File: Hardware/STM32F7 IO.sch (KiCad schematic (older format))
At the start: 26 parts, among them U16 STM32F765ZGT6

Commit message: Fixed serge suggestions
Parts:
- added TP?: TEST, Measurement_Points:Measurement_Point_Round-SMD-Pad_Big, symbol TEST
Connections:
- wire segments 183 -> 184
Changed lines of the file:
@@
 $Descr A4 11693 8268
 encoding utf-8
-Sheet 17 20
+Sheet 17 21
 Title "Autopilot Controller I/O"
 Date "2017-05-14"
@@
 $EndComp
 $Comp
-L GND #PWR48
+L GND #PWR046
 U 1 1 591E59BE
 P 10600 6000
-F 0 "#PWR48" H 10600 5750 50  0001 C CNN
+F 0 "#PWR046" H 10600 5750 50  0001 C CNN
 F 1 "GND" H 10600 5850 50  0000 C CNN
 F 2 "" H 10600 6000 50  0001 C CNN
@@
 $EndComp
 $Comp
-L GND #PWR46
+L GND #PWR047
 U 1 1 591EB43A
 P 6650 6500
-F 0 "#PWR46" H 6650 6250 50  0001 C CNN
+F 0 "#PWR047" H 6650 6250 50  0001 C CNN
 F 1 "GND" H 6650 6350 50  0000 C CNN
 F 2 "" H 6650 6500 50  0001 C CNN
@@
 Connection ~ 8550 2550
 $Comp
-L GND #PWR47
+L GND #PWR048
 U 1 1 59530E80
 P 8550 2600
-F 0 "#PWR47" H 8550 2350 50  0001 C CNN
+F 0 "#PWR048" H 8550 2350 50  0001 C CNN
 F 1 "GND" H 8550 2450 50  0000 C CNN
 F 2 "" H 8550 2600 50  0001 C CNN
@@
 L STM32F765ZGT6 U16
 U 8 1 595F8E91
-P 9500 5050
-F 0 "U16" H 9500 5950 60  0000 C CNN
-F 1 "STM32F765ZGT6" H 9500 5800 60  0000 C CNN
-F 2 "Housings_QFP:LQFP-144_20x20mm_Pitch0.5mm" H 10550 5150 60  0001 C CNN
-F 3 "" H 10550 5150 60  0001 C CNN
-F 4 "CHIP-001" H 9600 6050 60  0000 C CNN "part_num"
-	8    9500 5050
-	1    0    0    -1
+P 9600 5050
+F 0 "U16" H 9600 5950 60  0000 C CNN
+F 1 "STM32F765ZGT6" H 9600 5800 60  0000 C CNN
+F 2 "Housings_QFP:LQFP-144_20x20mm_Pitch0.5mm" H 10650 5150 60  0001 C CNN
+F 3 "" H 10650 5150 60  0001 C CNN
+F 4 "CHIP-001" H 9700 6050 60  0000 C CNN "part_num"
+	8    9600 5050
+	-1   0    0    -1
 $EndComp
 $Comp
@@
 	1    0    0    -1
 $EndComp
+$Comp
+L TEST TP?
+U 1 1 596A0986
+P 10450 2900
+F 0 "TP?" H 10450 3200 50  0000 C BNN
+F 1 "TEST" H 10450 3150 50  0000 C CNN
+F 2 "Measurement_Points:Measurement_Point_Round-SMD-Pad_Big" H 10450 2900 50  0001 C CNN
+F 3 "" H 10450 2900 50  0001 C CNN
+	1    10450 2900
+	1    0    0    -1
+$EndComp
+Wire Wire Line
+	10450 2900 10050 2900
 $EndSCHEMATC

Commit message: commit before my computer restarts
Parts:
- gave numbers to parts that had none: 1
- renumbered D17 to D15, D18 to D16, D19 to D17, R78 to R36, R79 to R37, R80 to R38, R81 to R39
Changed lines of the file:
@@
 VDD
 $Comp
-L LED D18
+L LED D16
 U 1 1 5952F90F
 P 8550 1950
-F 0 "D18" H 8550 2050 50  0000 C CNN
+F 0 "D16" H 8550 2050 50  0000 C CNN
 F 1 "LED" H 8550 1850 50  0000 C CNN
 F 2 "LEDs:LED_0603" H 8550 1950 50  0001 C CNN
@@
 $EndComp
 $Comp
-L LED D19
+L LED D17
 U 1 1 5952FA63
 P 8800 1950
-F 0 "D19" H 8800 2050 50  0000 C CNN
+F 0 "D17" H 8800 2050 50  0000 C CNN
 F 1 "LED" H 8800 1850 50  0000 C CNN
 F 2 "LEDs:LED_0603" H 8800 1950 50  0001 C CNN
@@
 $EndComp
 $Comp
-L LED D17
+L LED D15
 U 1 1 5952FAD9
 P 8300 1950
-F 0 "D17" H 8300 2050 50  0000 C CNN
+F 0 "D15" H 8300 2050 50  0000 C CNN
 F 1 "LED" H 8300 1850 50  0000 C CNN
 F 2 "LEDs:LED_0603" H 8300 1950 50  0001 C CNN
@@
 	7500 1450 7050 1450
 $Comp
-L R R78
+L R R36
 U 1 1 59530176
 P 8300 2300
-F 0 "R78" V 8380 2300 50  0000 C CNN
+F 0 "R36" V 8380 2300 50  0000 C CNN
 F 1 "100" V 8300 2300 50  0000 C CNN
 F 2 "Resistors_SMD:R_0603_HandSoldering" V 8230 2300 50  0001 C CNN
@@
 $EndComp
 $Comp
-L R R79
+L R R37
 U 1 1 5959BB88
 P 8550 2300
-F 0 "R79" V 8630 2300 50  0000 C CNN
+F 0 "R37" V 8630 2300 50  0000 C CNN
 F 1 "100" V 8550 2300 50  0000 C CNN
 F 2 "Resistors_SMD:R_0603_HandSoldering" V 8480 2300 50  0001 C CNN
@@
 $EndComp
 $Comp
-L R R80
+L R R38
 U 1 1 5959BBE4
 P 8800 2300
-F 0 "R80" V 8880 2300 50  0000 C CNN
+F 0 "R38" V 8880 2300 50  0000 C CNN
 F 1 "100" V 8800 2300 50  0000 C CNN
 F 2 "Resistors_SMD:R_0603_HandSoldering" V 8730 2300 50  0001 C CNN
@@
 $EndComp
 $Comp
-L R R81
+L R R39
 U 1 1 595F2290
 P 10550 3000
-F 0 "R81" V 10630 3000 50  0000 C CNN
+F 0 "R39" V 10630 3000 50  0000 C CNN
 F 1 "0" V 10550 3000 50  0000 C CNN
 F 2 "Resistors_SMD:R_0603_HandSoldering" V 10480 3000 50  0001 C CNN
@@
 $EndComp
 $Comp
-L TEST TP?
+L TEST TP39
 U 1 1 596A0986
 P 10450 2900
-F 0 "TP?" H 10450 3200 50  0000 C BNN
+F 0 "TP39" H 10450 3200 50  0000 C BNN
 F 1 "TEST" H 10450 3150 50  0000 C CNN
 F 2 "Measurement_Points:Measurement_Point_Round-SMD-Pad_Big" H 10450 2900 50  0001 C CNN

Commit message: routed PWM and SEL bus
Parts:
- TP39: footprint Measurement_Points:Measurement_Point_Round-SMD-Pad_Big -> Measurement_Points:Measurement_Point_Round-SMD-Pad_Small
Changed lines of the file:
@@
 F 0 "TP39" H 10450 3200 50  0000 C BNN
 F 1 "TEST" H 10450 3150 50  0000 C CNN
-F 2 "Measurement_Points:Measurement_Point_Round-SMD-Pad_Big" H 10450 2900 50  0001 C CNN
+F 2 "Measurement_Points:Measurement_Point_Round-SMD-Pad_Small" H 10450 2900 50  0001 C CNN
 F 3 "" H 10450 2900 50  0001 C CNN
 	1    10450 2900

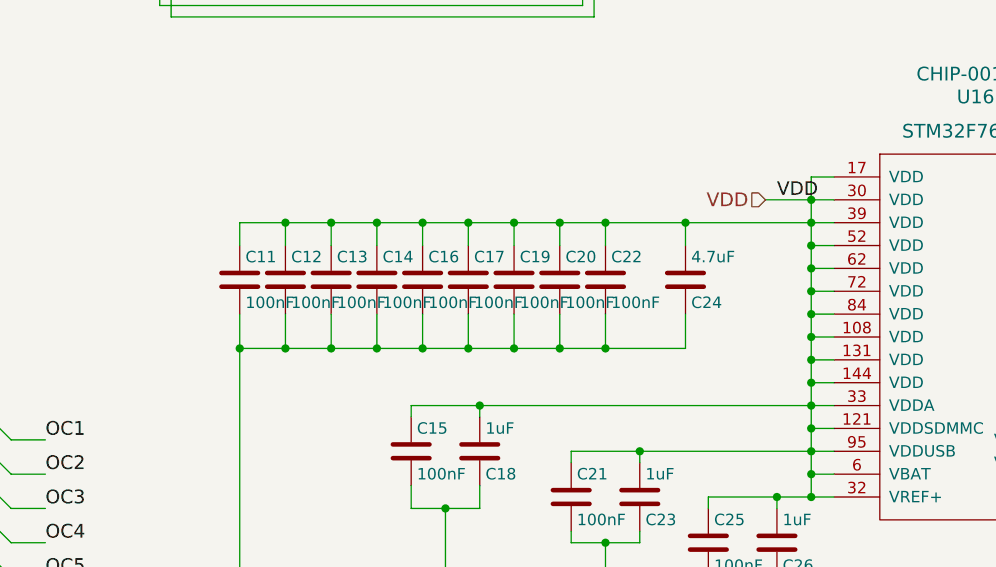
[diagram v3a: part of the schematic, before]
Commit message: placed headers in roughly correct spot
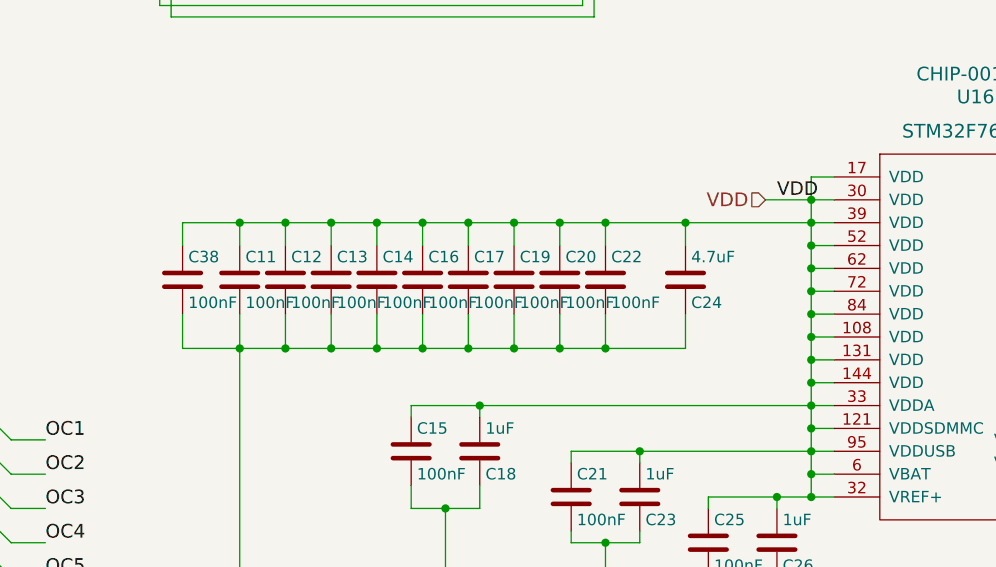
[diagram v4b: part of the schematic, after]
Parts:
- added C38: 100nF, Resistors_SMD:R_0603_HandSoldering, symbol C
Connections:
- net GND: now also C38.2
- net VDD: now also C38.1
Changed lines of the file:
@@
 	7950 5250 7950 5100
 Wire Wire Line
-	6350 5250 8300 5250
+	6100 5250 8300 5250
 Wire Wire Line
 	6350 5100 6350 6350
@@
 Connection ~ 8850 5300
 Wire Wire Line
-	6350 4700 8950 4700
+	6100 4700 8950 4700
 Connection ~ 8850 5400
 Wire Wire Line
@@
 Wire Wire Line
 	10450 2900 10050 2900
+$Comp
+L C C38
+U 1 1 592EA63D
+P 6100 4950
+F 0 "C38" H 6125 5050 50  0000 L CNN
+F 1 "100nF" H 6125 4850 50  0000 L CNN
+F 2 "Resistors_SMD:R_0603_HandSoldering" H 6138 4800 50  0001 C CNN
+F 3 "" H 6100 4950 50  0001 C CNN
+F 4 "CAPP-005" H 6100 4950 60  0001 C CNN "part_num"
+	1    6100 4950
+	1    0    0    -1
+$EndComp
+Wire Wire Line
+	6100 4700 6100 4800
+Connection ~ 6350 4700
+Wire Wire Line
+	6100 5100 6100 5250
 $EndSCHEMATC

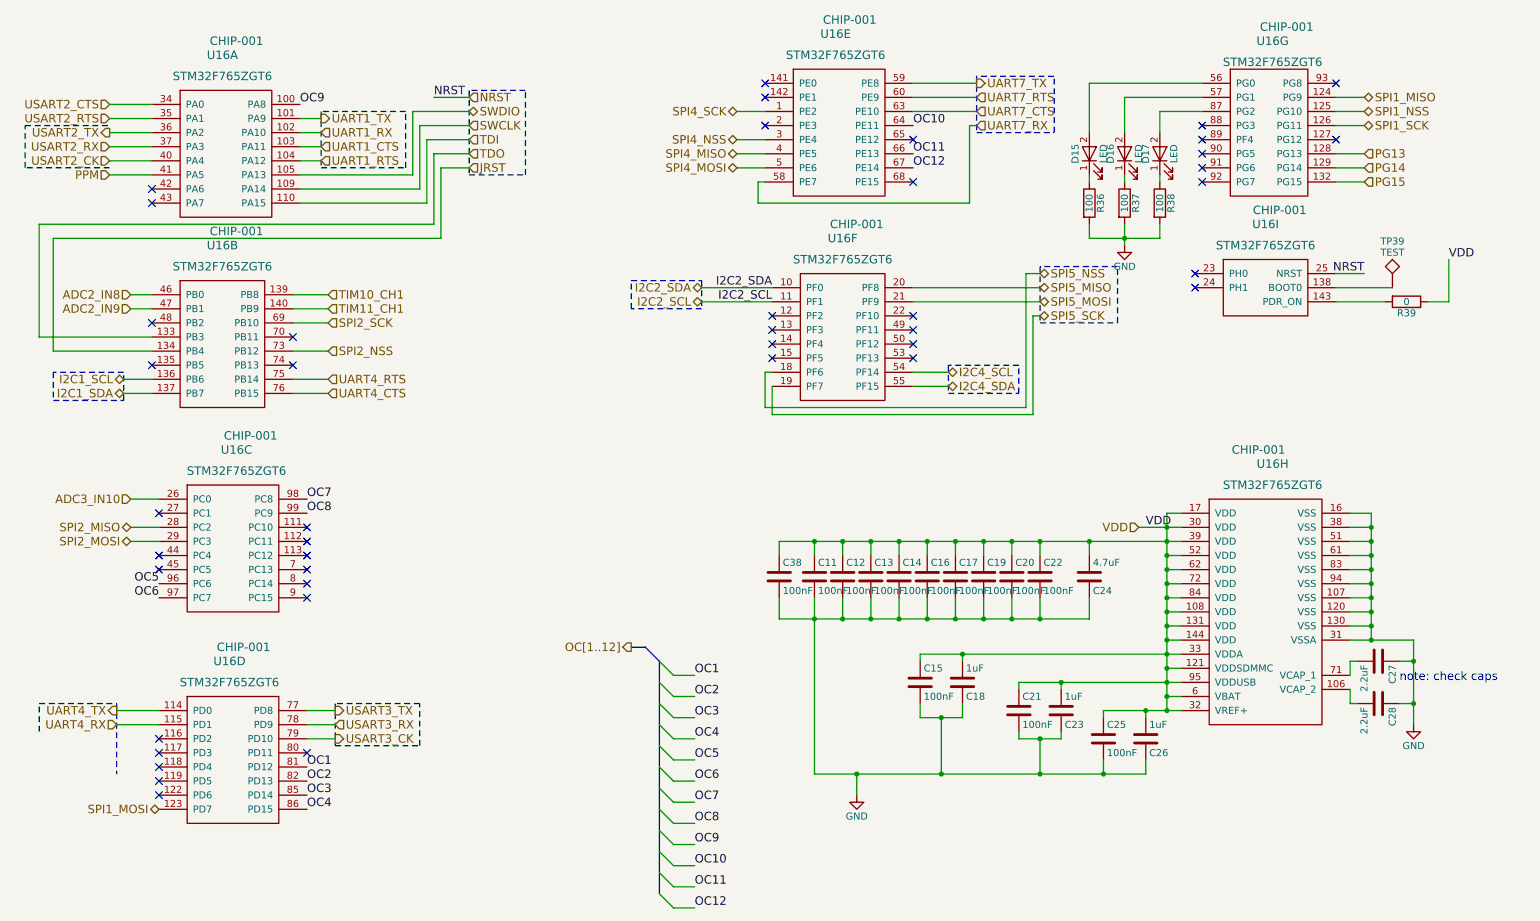
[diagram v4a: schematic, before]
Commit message: adc routing, made board smaller
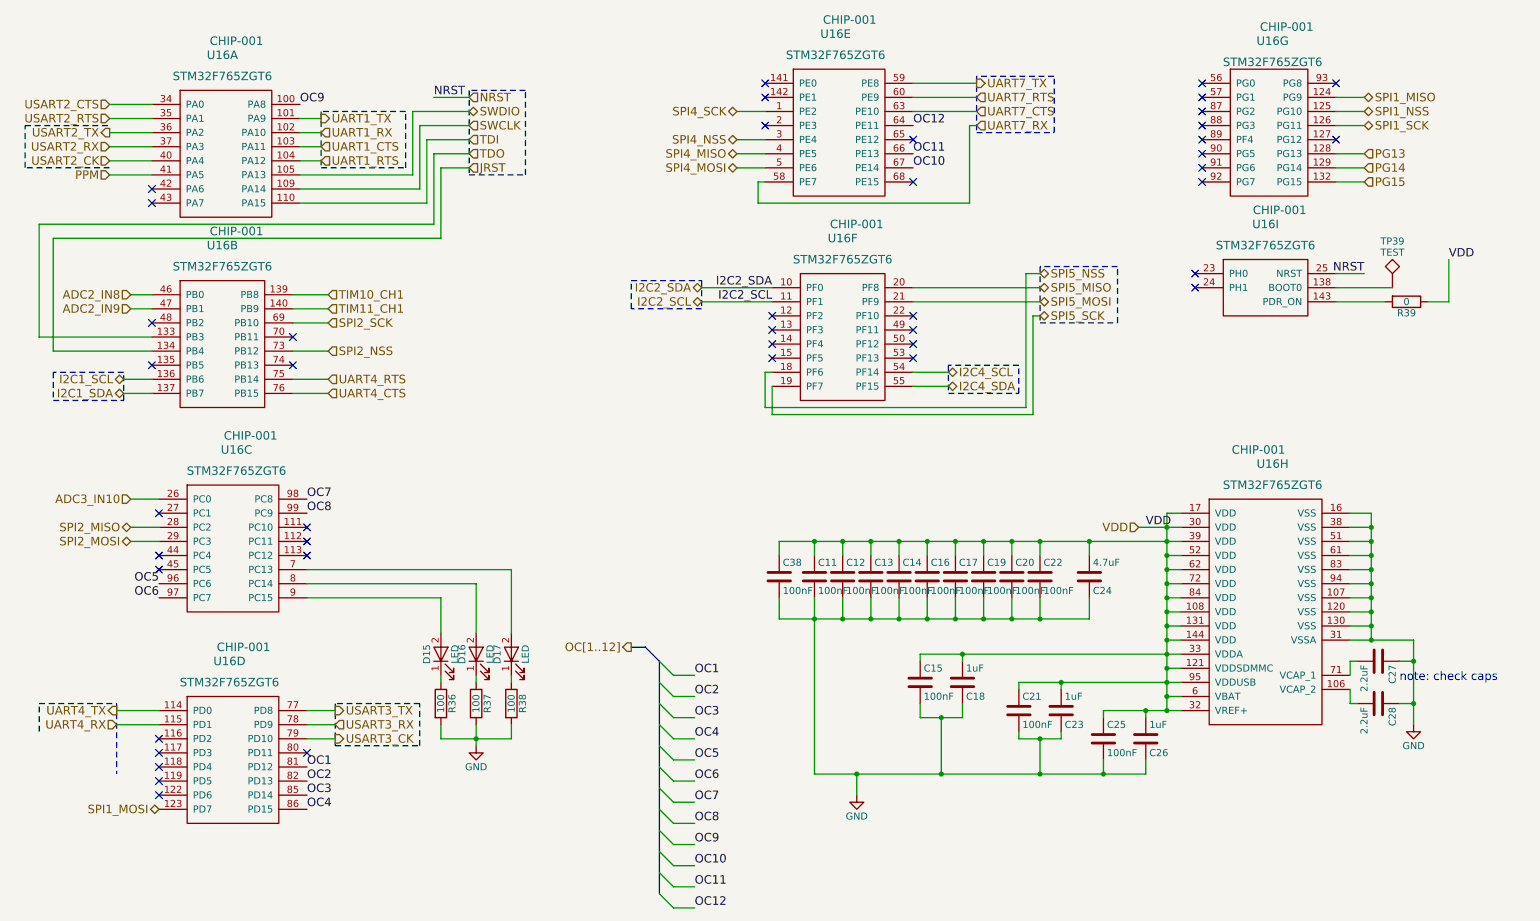
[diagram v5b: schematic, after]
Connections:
- net OC10: now also U16.67 (PE14); no longer U16.64 (PE11)
- net OC12: now also U16.64 (PE11); no longer U16.67 (PE14)
- net at D16.2 (A): now also U16.8 (PC14); no longer U16.57 (PG1)
- net at D17.2 (A): now also U16.7 (PC13); no longer U16.87 (PG2)
- net at D15.2 (A): now also U16.9 (PC15); no longer U16.56 (PG0)
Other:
- moved on the sheet: D15, D16, D17, R36, R37, R38
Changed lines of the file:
@@
 Text Label 2700 1600 0    60   ~ 0
 OC9
-Text Label 7050 1750 0    60   ~ 0
+Text Label 7050 2050 0    60   ~ 0
 OC10
 Text Label 7050 1950 0    60   ~ 0
 OC11
-Text Label 7050 2050 0    60   ~ 0
+Text Label 7050 1750 0    60   ~ 0
 OC12
 Text HLabel 1350 2100 0    60   Input ~ 0
@@
 NoConn ~ 2650 3250
 NoConn ~ 2650 3450
-NoConn ~ 2750 5100
-NoConn ~ 2750 5000
-NoConn ~ 2750 4900
 NoConn ~ 2750 4800
 NoConn ~ 2750 4700
@@
 L LED D16
 U 1 1 5952F90F
-P 8550 1950
-F 0 "D16" H 8550 2050 50  0000 C CNN
-F 1 "LED" H 8550 1850 50  0000 C CNN
-F 2 "LEDs:LED_0603" H 8550 1950 50  0001 C CNN
-F 3 "" H 8550 1950 50  0001 C CNN
-F 4 "DIOD-002" H 8550 1950 60  0001 C CNN "part_num"
-	1    8550 1950
+P 3950 5500
+F 0 "D16" H 3950 5600 50  0000 C CNN
+F 1 "LED" H 3950 5400 50  0000 C CNN
+F 2 "LEDs:LED_0603" H 3950 5500 50  0001 C CNN
+F 3 "" H 3950 5500 50  0001 C CNN
+F 4 "DIOD-002" H 3950 5500 60  0001 C CNN "part_num"
+	1    3950 5500
 	0    -1   -1   0
 $EndComp
@@
 L LED D17
 U 1 1 5952FA63
-P 8800 1950
-F 0 "D17" H 8800 2050 50  0000 C CNN
-F 1 "LED" H 8800 1850 50  0000 C CNN
-F 2 "LEDs:LED_0603" H 8800 1950 50  0001 C CNN
-F 3 "" H 8800 1950 50  0001 C CNN
-F 4 "DIOD-002" H 8800 1950 60  0001 C CNN "part_num"
-	1    8800 1950
+P 4200 5500
+F 0 "D17" H 4200 5600 50  0000 C CNN
+F 1 "LED" H 4200 5400 50  0000 C CNN
+F 2 "LEDs:LED_0603" H 4200 5500 50  0001 C CNN
+F 3 "" H 4200 5500 50  0001 C CNN
+F 4 "DIOD-002" H 4200 5500 60  0001 C CNN "part_num"
+	1    4200 5500
 	0    -1   -1   0
 $EndComp
@@
 L LED D15
 U 1 1 5952FAD9
-P 8300 1950
-F 0 "D15" H 8300 2050 50  0000 C CNN
-F 1 "LED" H 8300 1850 50  0000 C CNN
-F 2 "LEDs:LED_0603" H 8300 1950 50  0001 C CNN
-F 3 "" H 8300 1950 50  0001 C CNN
-F 4 "DIOD-002" H 8300 1950 60  0001 C CNN "part_num"
-	1    8300 1950
+P 3700 5500
+F 0 "D15" H 3700 5600 50  0000 C CNN
+F 1 "LED" H 3700 5400 50  0000 C CNN
+F 2 "LEDs:LED_0603" H 3700 5500 50  0001 C CNN
+F 3 "" H 3700 5500 50  0001 C CNN
+F 4 "DIOD-002" H 3700 5500 60  0001 C CNN "part_num"
+	1    3700 5500
 	0    -1   -1   0
 $EndComp
@@
 L R R36
 U 1 1 59530176
-P 8300 2300
-F 0 "R36" V 8380 2300 50  0000 C CNN
-F 1 "100" V 8300 2300 50  0000 C CNN
-F 2 "Resistors_SMD:R_0603_HandSoldering" V 8230 2300 50  0001 C CNN
-F 3 "" H 8300 2300 50  0001 C CNN
-F 4 "RESS-006" V 8300 2300 60  0001 C CNN "part_num"
-	1    8300 2300
-	1    0    0    -1
-$EndComp
-Wire Wire Line
-	8300 2150 8300 2100
-Wire Wire Line
-	8550 2100 8550 2150
-Wire Wire Line
-	8800 2150 8800 2100
-Wire Wire Line
-	8800 1800 8800 1650
-Wire Wire Line
-	8800 1650 9100 1650
-Wire Wire Line
-	8550 1800 8550 1550
-Wire Wire Line
-	8550 1550 9100 1550
-Wire Wire Line
-	8300 1800 8300 1450
-Wire Wire Line
-	8300 1450 9100 1450
-Wire Wire Line
-	8300 2450 8300 2550
-Wire Wire Line
-	8300 2550 8800 2550
-Wire Wire Line
-	8800 2550 8800 2450
-Wire Wire Line
-	8550 2450 8550 2600
-Connection ~ 8550 2550
+P 3700 5850
+F 0 "R36" V 3780 5850 50  0000 C CNN
+F 1 "100" V 3700 5850 50  0000 C CNN
+F 2 "Resistors_SMD:R_0603_HandSoldering" V 3630 5850 50  0001 C CNN
+F 3 "" H 3700 5850 50  0001 C CNN
+F 4 "RESS-006" V 3700 5850 60  0001 C CNN "part_num"
+	1    3700 5850
+	1    0    0    -1
+$EndComp
+Wire Wire Line
+	3700 5700 3700 5650
+Wire Wire Line
+	3950 5650 3950 5700
+Wire Wire Line
+	4200 5700 4200 5650
+Wire Wire Line
+	3700 6000 3700 6100
+Wire Wire Line
+	3700 6100 4200 6100
+Wire Wire Line
+	4200 6100 4200 6000
+Wire Wire Line
+	3950 6000 3950 6150
+Connection ~ 3950 6100
 $Comp
 L GND #PWR048
 U 1 1 59530E80
-P 8550 2600
-F 0 "#PWR048" H 8550 2350 50  0001 C CNN
-F 1 "GND" H 8550 2450 50  0000 C CNN
-F 2 "" H 8550 2600 50  0001 C CNN
-F 3 "" H 8550 2600 50  0001 C CNN
-	1    8550 2600
+P 3950 6150
+F 0 "#PWR048" H 3950 5900 50  0001 C CNN
+F 1 "GND" H 3950 6000 50  0000 C CNN
+F 2 "" H 3950 6150 50  0001 C CNN
+F 3 "" H 3950 6150 50  0001 C CNN
+	1    3950 6150
 	1    0    0    -1
 $EndComp
@@
 L R R37
 U 1 1 5959BB88
-P 8550 2300
-F 0 "R37" V 8630 2300 50  0000 C CNN
-F 1 "100" V 8550 2300 50  0000 C CNN
-F 2 "Resistors_SMD:R_0603_HandSoldering" V 8480 2300 50  0001 C CNN
-F 3 "" H 8550 2300 50  0001 C CNN
-F 4 "RESS-006" V 8550 2300 60  0001 C CNN "part_num"
-	1    8550 2300
+P 3950 5850
+F 0 "R37" V 4030 5850 50  0000 C CNN
+F 1 "100" V 3950 5850 50  0000 C CNN
+F 2 "Resistors_SMD:R_0603_HandSoldering" V 3880 5850 50  0001 C CNN
+F 3 "" H 3950 5850 50  0001 C CNN
+F 4 "RESS-006" V 3950 5850 60  0001 C CNN "part_num"
+	1    3950 5850
 	1    0    0    -1
 $EndComp
@@
 L R R38
 U 1 1 5959BBE4
-P 8800 2300
-F 0 "R38" V 8880 2300 50  0000 C CNN
-F 1 "100" V 8800 2300 50  0000 C CNN
-F 2 "Resistors_SMD:R_0603_HandSoldering" V 8730 2300 50  0001 C CNN
-F 3 "" H 8800 2300 50  0001 C CNN
-F 4 "RESS-006" V 8800 2300 60  0001 C CNN "part_num"
-	1    8800 2300
+P 4200 5850
+F 0 "R38" V 4280 5850 50  0000 C CNN
+F 1 "100" V 4200 5850 50  0000 C CNN
+F 2 "Resistors_SMD:R_0603_HandSoldering" V 4130 5850 50  0001 C CNN
+F 3 "" H 4200 5850 50  0001 C CNN
+F 4 "RESS-006" V 4200 5850 60  0001 C CNN "part_num"
+	1    4200 5850
 	1    0    0    -1
 $EndComp
@@
 Wire Wire Line
 	6100 5100 6100 5250
+Wire Wire Line
+	3700 5100 3700 5350
+Wire Wire Line
+	3700 5100 2750 5100
+Wire Wire Line
+	2750 5000 3950 5000
+Wire Wire Line
+	3950 5000 3950 5350
+Wire Wire Line
+	2750 4900 4200 4900
+Wire Wire Line
+	4200 4900 4200 5350
+NoConn ~ 9100 1450
+NoConn ~ 9100 1550
+NoConn ~ 9100 1650
 $EndSCHEMATC
